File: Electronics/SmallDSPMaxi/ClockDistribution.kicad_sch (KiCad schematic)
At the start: 16 parts, among them U15 PL123-09OC

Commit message: Fixes minor issues
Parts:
- removed R31: 1k, Resistor_SMD:R_0402_1005Metric, symbol Device:R_Small
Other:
- note added: "Clock Buffer"
- company: (none) -> Till Heuer
- title: (none) -> SmallDSP Maxi
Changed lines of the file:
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@@
 (kicad_sch (version 20230121) (generator eeschema)
   (paper "A4")
-  (junction (at 109.22 85.09) (diameter 0) (color 0 0 0 0)
+  (title_block
+    (title "SmallDSP Maxi")
+    (date "2023-11-05")
+    (rev "1.0")
+    (company "Till Heuer")
   )
   (wire (pts (xy 152.4 93.98) (xy 156.21 93.98))
@@
     (stroke (width 0) (type default))
   )
-  (wire (pts (xy 109.22 92.71) (xy 109.22 93.98))
-    (stroke (width 0) (type default))
-  )
   (wire (pts (xy 149.86 60.96) (xy 149.86 62.23))
     (stroke (width 0) (type default))
@@
     (stroke (width 0) (type default))
   )
-  (wire (pts (xy 109.22 85.09) (xy 109.22 87.63))
-    (stroke (width 0) (type default))
-  )
   (wire (pts (xy 152.4 101.6) (xy 156.21 101.6))
     (stroke (width 0) (type default))
@@
   (wire (pts (xy 152.4 88.9) (xy 156.21 88.9))
     (stroke (width 0) (type default))
+  )
+  (text "Clock Buffer" (at 48.26 49.53 0)
+    (effects (font (face "Helvetica Neue") (size 5 5) (thickness 1) bold) (justify left bottom))
   )
   (hierarchical_label "MCLK Out 4" (shape output) (at 166.37 106.68 0) (fields_autoplaced)
@@
     )
   )
-  (symbol (lib_id "Device:R_Small") (at 109.22 90.17 0) (unit 1)
-    (in_bom yes) (on_board yes) (dnp yes) (fields_autoplaced)
-    (property "Reference" "R31" (at 110.7186 88.9579 0)
-      (effects (font (size 1.27 1.27)) (justify left))
-    )
-    (property "Value" "1k" (at 110.7186 91.3821 0)
-      (effects (font (size 1.27 1.27)) (justify left))
-    )
-    (property "Footprint" "Resistor_SMD:R_0402_1005Metric" (at 109.22 90.17 0)
-      (effects (font (size 1.27 1.27)) hide)
-    )
-    (property "Datasheet" "~" (at 109.22 90.17 0)
-      (effects (font (size 1.27 1.27)) hide)
-    )
-    (property "Dielectric" "" (at 109.22 90.17 0)
-      (effects (font (size 1.27 1.27)) hide)
-    )
-    (property "Notes" "" (at 109.22 90.17 0)
-      (effects (font (size 1.27 1.27)) hide)
-    )
-    (property "Rated Voltage" "" (at 109.22 90.17 0)
-      (effects (font (size 1.27 1.27)) hide)
-    )
-    (property "Assembling" "X" (at 109.22 90.17 0)
-      (effects (font (size 1.27 1.27)) hide)
-    )
-    (property "Manufacturer" "UNI-ROYAL(Uniroyal Elec)" (at 109.22 90.17 0)
-      (effects (font (size 1.27 1.27)) hide)
-    )
-    (property "Part Number" "0402WGF1001TCE" (at 109.22 90.17 0)
-      (effects (font (size 1.27 1.27)) hide)
-    )
-    (property "Rated Power" "62.5mW" (at 109.22 90.17 0)
-      (effects (font (size 1.27 1.27)) hide)
-    )
-    (property "Rated Current" "" (at 109.22 90.17 0)
-      (effects (font (size 1.27 1.27)) hide)
-    )
-    (property "Tolerance" "1%" (at 109.22 90.17 0)
-      (effects (font (size 1.27 1.27)) hide)
-    )
-    (property "LCSC Part #" "C11702" (at 109.22 90.17 0)
-      (effects (font (size 1.27 1.27)) hide)
-    )
-    (pin "1")
-    (pin "2")
-    (instances
-      (project "SmallDSPMaxi"
-        (path "/5f2729b5-edcd-4fbc-b3fb-44096724c941"
-          (reference "R31") (unit 1)
-        )
-        (path "/5f2729b5-edcd-4fbc-b3fb-44096724c941/31216c34-c913-473d-81bf-549ca7aee41d"
-          (reference "R90") (unit 1)
-        )
-      )
-    )
-  )
   (symbol (lib_id "Device:R_Small") (at 158.75 104.14 90) (unit 1)
     (in_bom yes) (on_board yes) (dnp no)
@@
         )
       )
-    )
-  )
-  (symbol (lib_id "power:GND") (at 109.22 93.98 0) (unit 1)
-    (in_bom yes) (on_board yes) (dnp no) (fields_autoplaced)
-    (property "Reference" "#PWR0384" (at 109.22 100.33 0)
-      (effects (font (size 1.27 1.27)) hide)
-    )
-    (property "Value" "GND" (at 109.22 99.06 0)
-      (effects (font (size 1.27 1.27)))
-    )
-    (property "Footprint" "" (at 109.22 93.98 0)
-      (effects (font (size 1.27 1.27)) hide)
-    )
-    (property "Datasheet" "" (at 109.22 93.98 0)
-      (effects (font (size 1.27 1.27)) hide)
-    )
-    (pin "1")
-    (instances
-      (project "SmallDSPMaxi"
-        (path "/5f2729b5-edcd-4fbc-b3fb-44096724c941/31216c34-c913-473d-81bf-549ca7aee41d"
-          (reference "#PWR0384") (unit 1)
-        )
-      )

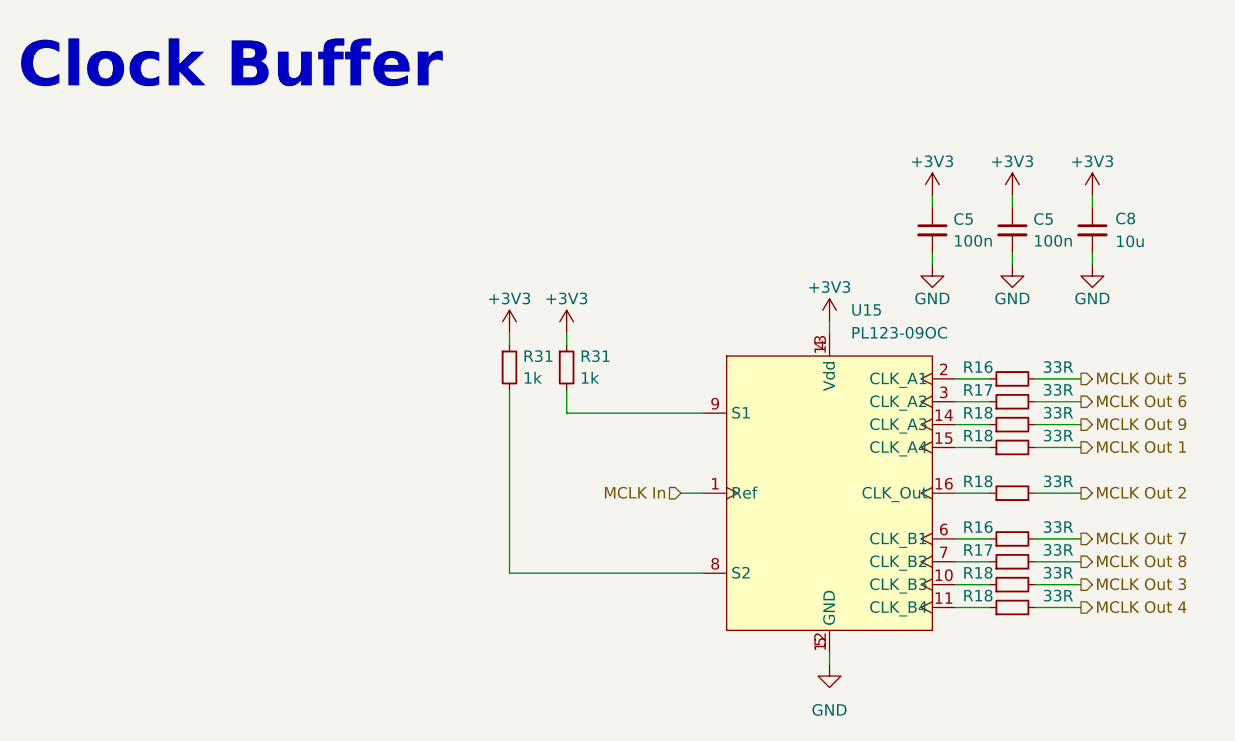
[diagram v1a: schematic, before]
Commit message: adds usb to i2s bridge to micro. Adds tweaks for layout of maxi.
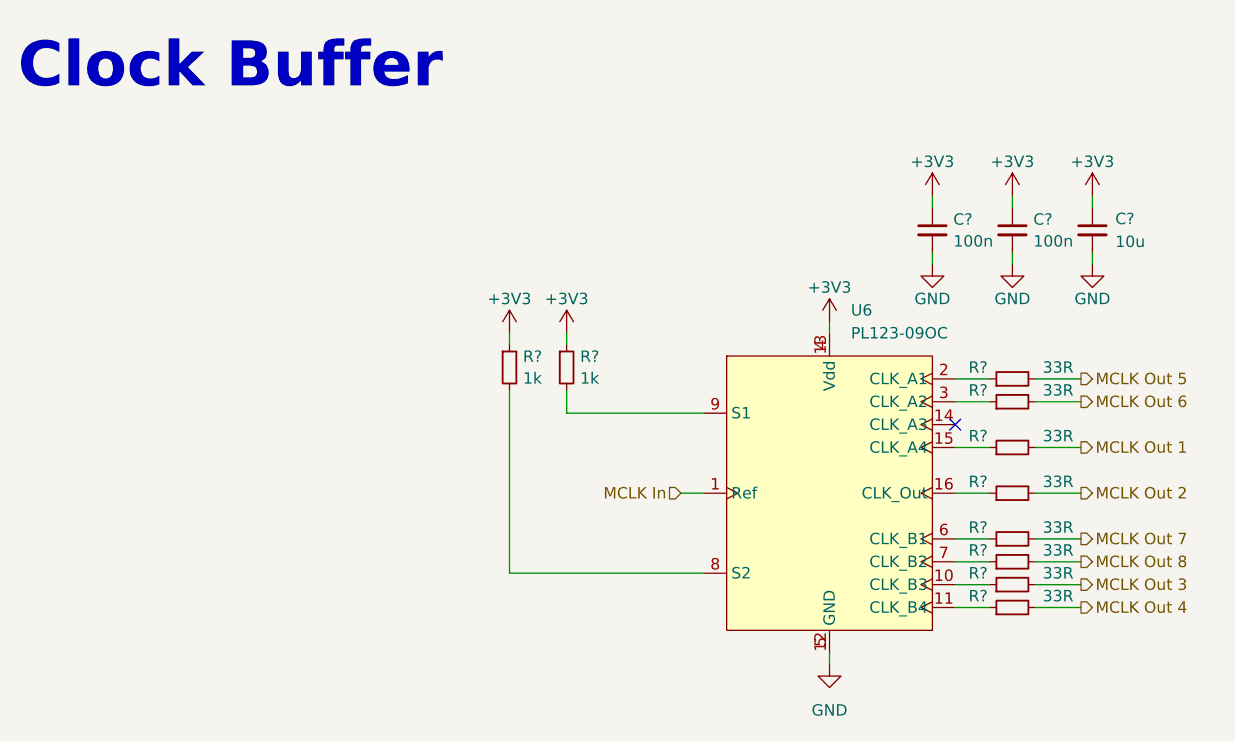
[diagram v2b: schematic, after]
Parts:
- removed R18: 33R, Resistor_SMD:R_0402_1005Metric, symbol Device:R_Small
- renumbered C8 to C?, C5 to C?, R31 to R?, R16 to R?, R18 to R?, R17 to R?, U15 to U6
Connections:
- no-connect marks 0 -> 1

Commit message: Adds final state of Maxi rev 1.0 and unbalanced IO boards rev 1.0.
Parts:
- U9: renamed from U6; LCSC Part # (none) -> -; Manufacturer (none) -> Microchip; Part Number (none) -> PL123-09OC
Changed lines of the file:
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@@
   (title_block
     (title "SmallDSP Maxi")
-    (date "2023-12-01")
+    (date "2024-01-06")
     (rev "1.0")
     (company "Till Heuer")
@@
         )
         (path "/5f2729b5-edcd-4fbc-b3fb-44096724c941/31216c34-c913-473d-81bf-549ca7aee41d"
-          (reference "R48") (unit 1)
+          (reference "R44") (unit 1)
         )
       )
@@
   (symbol (lib_id "1_Project_Symbols:PL123-09OC") (at 138.43 93.98 0) (unit 1)
     (in_bom yes) (on_board yes) (dnp no) (fields_autoplaced)
-    (property "Reference" "U6" (at 140.803 73.66 0)
+    (property "Reference" "U9" (at 140.803 73.66 0)
       (effects (font (size 1.27 1.27)) (justify left))
     )
@@
     )
     (property "Datasheet" "" (at 138.43 78.74 0)
+      (effects (font (size 1.27 1.27)) hide)
+    )
+    (property "LCSC Part #" "-" (at 138.43 93.98 0)
+      (effects (font (size 1.27 1.27)) hide)
+    )
+    (property "Manufacturer" "Microchip" (at 138.43 93.98 0)
+      (effects (font (size 1.27 1.27)) hide)
+    )
+    (property "Part Number" "PL123-09OC" (at 138.43 93.98 0)
       (effects (font (size 1.27 1.27)) hide)
     )
@@
       (project "SmallDSPMaxi"
         (path "/5f2729b5-edcd-4fbc-b3fb-44096724c941/31216c34-c913-473d-81bf-549ca7aee41d"
-          (reference "U6") (unit 1)
+          (reference "U9") (unit 1)
         )
       )
@@
         )
         (path "/5f2729b5-edcd-4fbc-b3fb-44096724c941/31216c34-c913-473d-81bf-549ca7aee41d"
-          (reference "R49") (unit 1)
+          (reference "R45") (unit 1)
         )
       )
@@
         )
         (path "/5f2729b5-edcd-4fbc-b3fb-44096724c941/31216c34-c913-473d-81bf-549ca7aee41d"
-          (reference "R56") (unit 1)
+          (reference "R52") (unit 1)
         )
       )
@@
         )
         (path "/5f2729b5-edcd-4fbc-b3fb-44096724c941/31216c34-c913-473d-81bf-549ca7aee41d"
-          (reference "R51") (unit 1)
+          (reference "R47") (unit 1)
         )
       )
@@
   (symbol (lib_id "power:GND") (at 138.43 113.03 0) (unit 1)
     (in_bom yes) (on_board yes) (dnp no) (fields_autoplaced)
-    (property "Reference" "#PWR0131" (at 138.43 119.38 0)
+    (property "Reference" "#PWR0122" (at 138.43 119.38 0)
       (effects (font (size 1.27 1.27)) hide)
     )
@@
       (project "SmallDSPMaxi"
         (path "/5f2729b5-edcd-4fbc-b3fb-44096724c941/31216c34-c913-473d-81bf-549ca7aee41d"
-          (reference "#PWR0131") (unit 1)
+          (reference "#PWR0122") (unit 1)
         )
       )
@@
         )
         (path "/5f2729b5-edcd-4fbc-b3fb-44096724c941/31216c34-c913-473d-81bf-549ca7aee41d"
-          (reference "#PWR0135") (unit 1)
+          (reference "#PWR0126") (unit 1)
         )
       )
@@
         )
         (path "/5f2729b5-edcd-4fbc-b3fb-44096724c941/31216c34-c913-473d-81bf-549ca7aee41d"
-          (reference "C45") (unit 1)
+          (reference "C47") (unit 1)
         )
       )
@@
         )
         (path "/5f2729b5-edcd-4fbc-b3fb-44096724c941/31216c34-c913-473d-81bf-549ca7aee41d"
-          (reference "R47") (unit 1)
+          (reference "R43") (unit 1)
         )
       )
@@
         )
         (path "/5f2729b5-edcd-4fbc-b3fb-44096724c941/31216c34-c913-473d-81bf-549ca7aee41d"
-          (reference "R55") (unit 1)
+          (reference "R51") (unit 1)
         )
       )
@@
         )
         (path "/5f2729b5-edcd-4fbc-b3fb-44096724c941/31216c34-c913-473d-81bf-549ca7aee41d"
-          (reference "R54") (unit 1)
+          (reference "R50") (unit 1)
         )
       )
@@
         )
         (path "/5f2729b5-edcd-4fbc-b3fb-44096724c941/31216c34-c913-473d-81bf-549ca7aee41d"
-          (reference "#PWR0137") (unit 1)
+          (reference "#PWR0128") (unit 1)
         )
       )
@@
         )
         (path "/5f2729b5-edcd-4fbc-b3fb-44096724c941/31216c34-c913-473d-81bf-549ca7aee41d"
-          (reference "R53") (unit 1)
+          (reference "R49") (unit 1)
         )
       )
@@
         )
         (path "/5f2729b5-edcd-4fbc-b3fb-44096724c941/31216c34-c913-473d-81bf-549ca7aee41d"
-          (reference "C43") (unit 1)
+          (reference "C45") (unit 1)
         )
       )
@@
         )
         (path "/5f2729b5-edcd-4fbc-b3fb-44096724c941/31216c34-c913-473d-81bf-549ca7aee41d"
-          (reference "R52") (unit 1)
+          (reference "R48") (unit 1)
         )
       )
@@
         )
         (path "/5f2729b5-edcd-4fbc-b3fb-44096724c941/31216c34-c913-473d-81bf-549ca7aee41d"
-          (reference "#PWR0128") (unit 1)
+          (reference "#PWR0119") (unit 1)
         )
       )
@@
         )
         (path "/5f2729b5-edcd-4fbc-b3fb-44096724c941/31216c34-c913-473d-81bf-549ca7aee41d"
-          (reference "#PWR0129") (unit 1)
+          (reference "#PWR0120") (unit 1)
         )
       )
@@
         )
         (path "/5f2729b5-edcd-4fbc-b3fb-44096724c941/31216c34-c913-473d-81bf-549ca7aee41d"
-          (reference "#PWR0132") (unit 1)
+          (reference "#PWR0123") (unit 1)
         )
       )
@@
         )
         (path "/5f2729b5-edcd-4fbc-b3fb-44096724c941/31216c34-c913-473d-81bf-549ca7aee41d"
-          (reference "R50") (unit 1)
+          (reference "R46") (unit 1)
         )
       )
@@
         )
         (path "/5f2729b5-edcd-4fbc-b3fb-44096724c941/31216c34-c913-473d-81bf-549ca7aee41d"
-          (reference "C44") (unit 1)
+          (reference "C46") (unit 1)
         )
       )
@@
         )
         (path "/5f2729b5-edcd-4fbc-b3fb-44096724c941/31216c34-c913-473d-81bf-549ca7aee41d"
-          (reference "#PWR0130") (unit 1)
+          (reference "#PWR0121") (unit 1)
         )
       )
@@
         )
         (path "/5f2729b5-edcd-4fbc-b3fb-44096724c941/31216c34-c913-473d-81bf-549ca7aee41d"
-          (reference "#PWR0134") (unit 1)
+          (reference "#PWR0125") (unit 1)
         )
       )
@@
         )
         (path "/5f2729b5-edcd-4fbc-b3fb-44096724c941/31216c34-c913-473d-81bf-549ca7aee41d"
-          (reference "#PWR0136") (unit 1)
+          (reference "#PWR0127") (unit 1)
         )
       )
@@
         )
         (path "/5f2729b5-edcd-4fbc-b3fb-44096724c941/31216c34-c913-473d-81bf-549ca7aee41d"
-          (reference "#PWR0133") (unit 1)
-        )
-      )
+          (reference "#PWR0124") (unit 1)
+        )
+      )

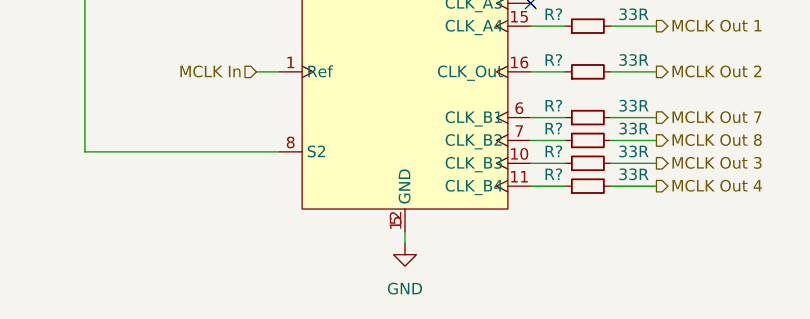
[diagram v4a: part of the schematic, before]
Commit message: Maxi: Replaces STM32 programming pin header with WE RedFit connectorand fixes minor issues. Adds driver for AKM AK4619 Codec and STM32CubeIDE workspace for Maxi firmware.
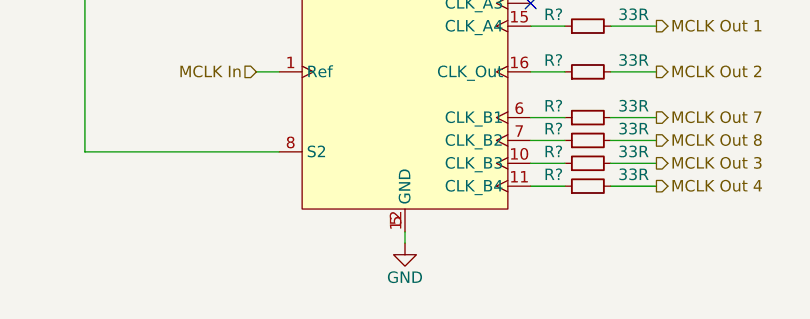
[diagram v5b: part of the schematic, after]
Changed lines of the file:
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@@
   (title_block
     (title "SmallDSP Maxi")
-    (date "2024-01-06")
-    (rev "1.0")
+    (date "2024-02-19")
+    (rev "1.1")
     (company "Till Heuer")
   )
@@
   )
   (symbol (lib_id "power:GND") (at 138.43 113.03 0) (unit 1)
-    (in_bom yes) (on_board yes) (dnp no) (fields_autoplaced)
+    (in_bom yes) (on_board yes) (dnp no)
     (property "Reference" "#PWR0122" (at 138.43 119.38 0)
       (effects (font (size 1.27 1.27)) hide)
     )
-    (property "Value" "GND" (at 138.43 118.11 0)
-      (effects (font (size 1.27 1.27)))
-    )
+    (property "Value" "GND" (at 138.43 116.84 0)
+      (effects (font (size 1.27 1.27)))
+    )

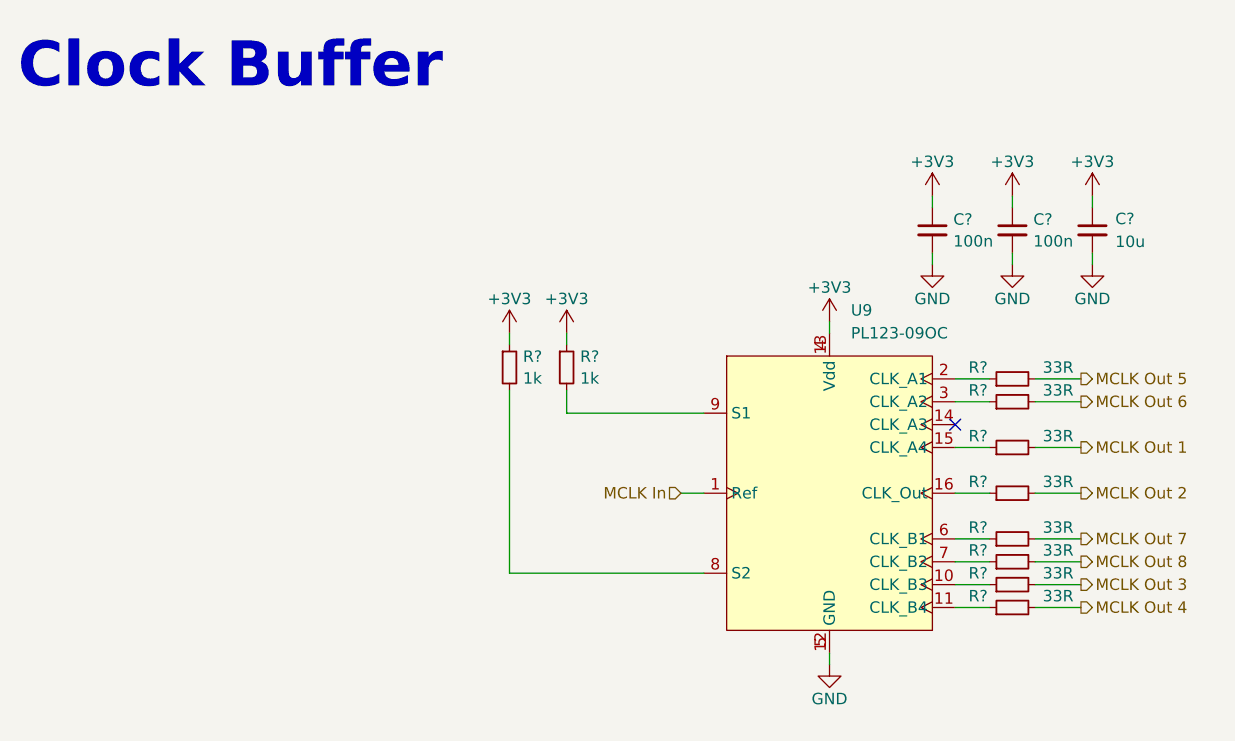
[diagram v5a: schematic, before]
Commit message: Adds AES17 measurements for rev1 of maxi. adds first iteration of maxi firmware. prototype now functional. adds mechanical information such as pcb 3d models and datasheets for psu and power switch, -connector.
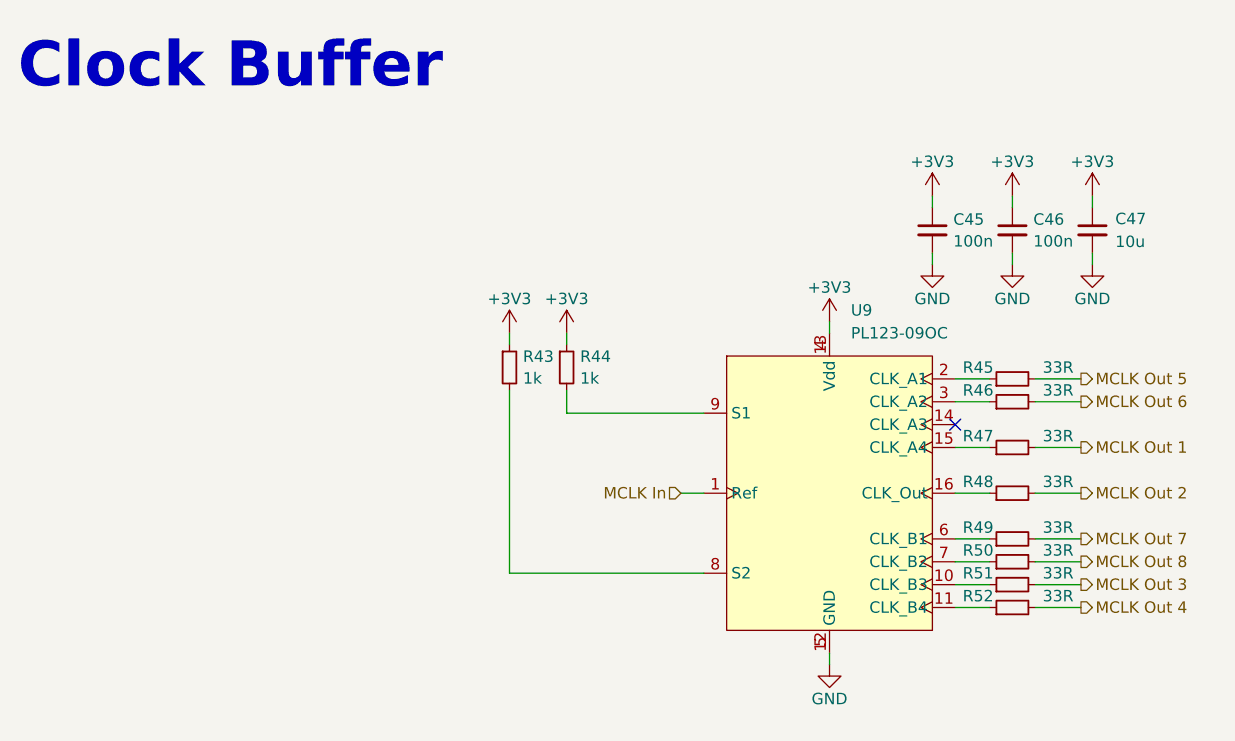
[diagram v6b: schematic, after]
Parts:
- gave numbers to parts that had none: 13
